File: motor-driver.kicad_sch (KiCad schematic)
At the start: 22 parts, among them J2 SIGNAL, J3 PWR, J4 RTMI, Q5 BSS138

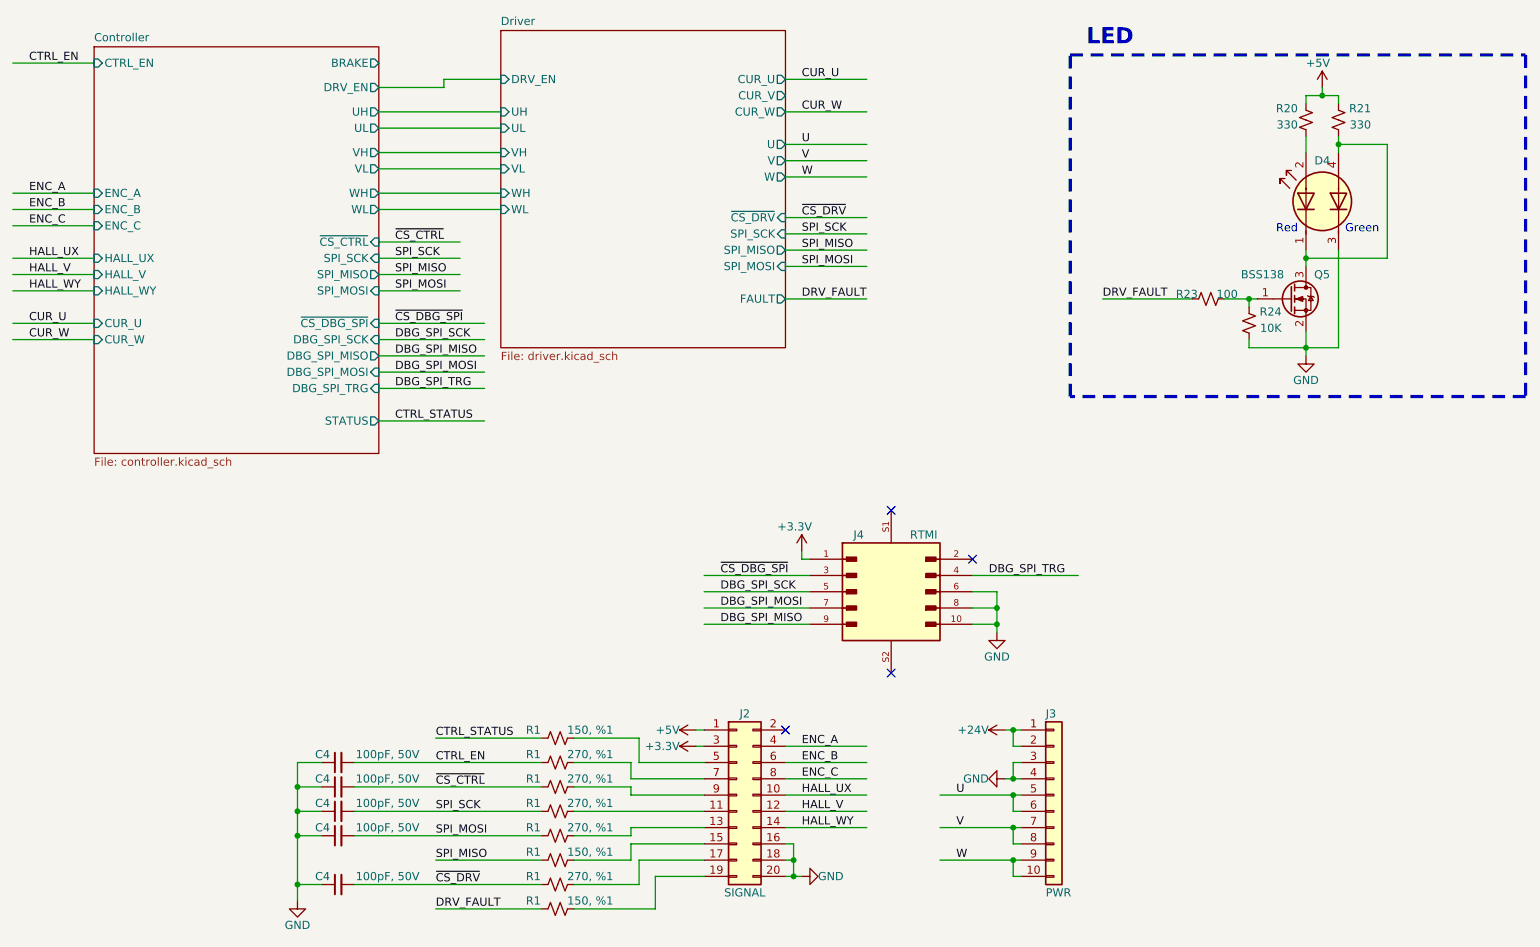
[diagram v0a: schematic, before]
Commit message: Applied the fixes to the pcb.
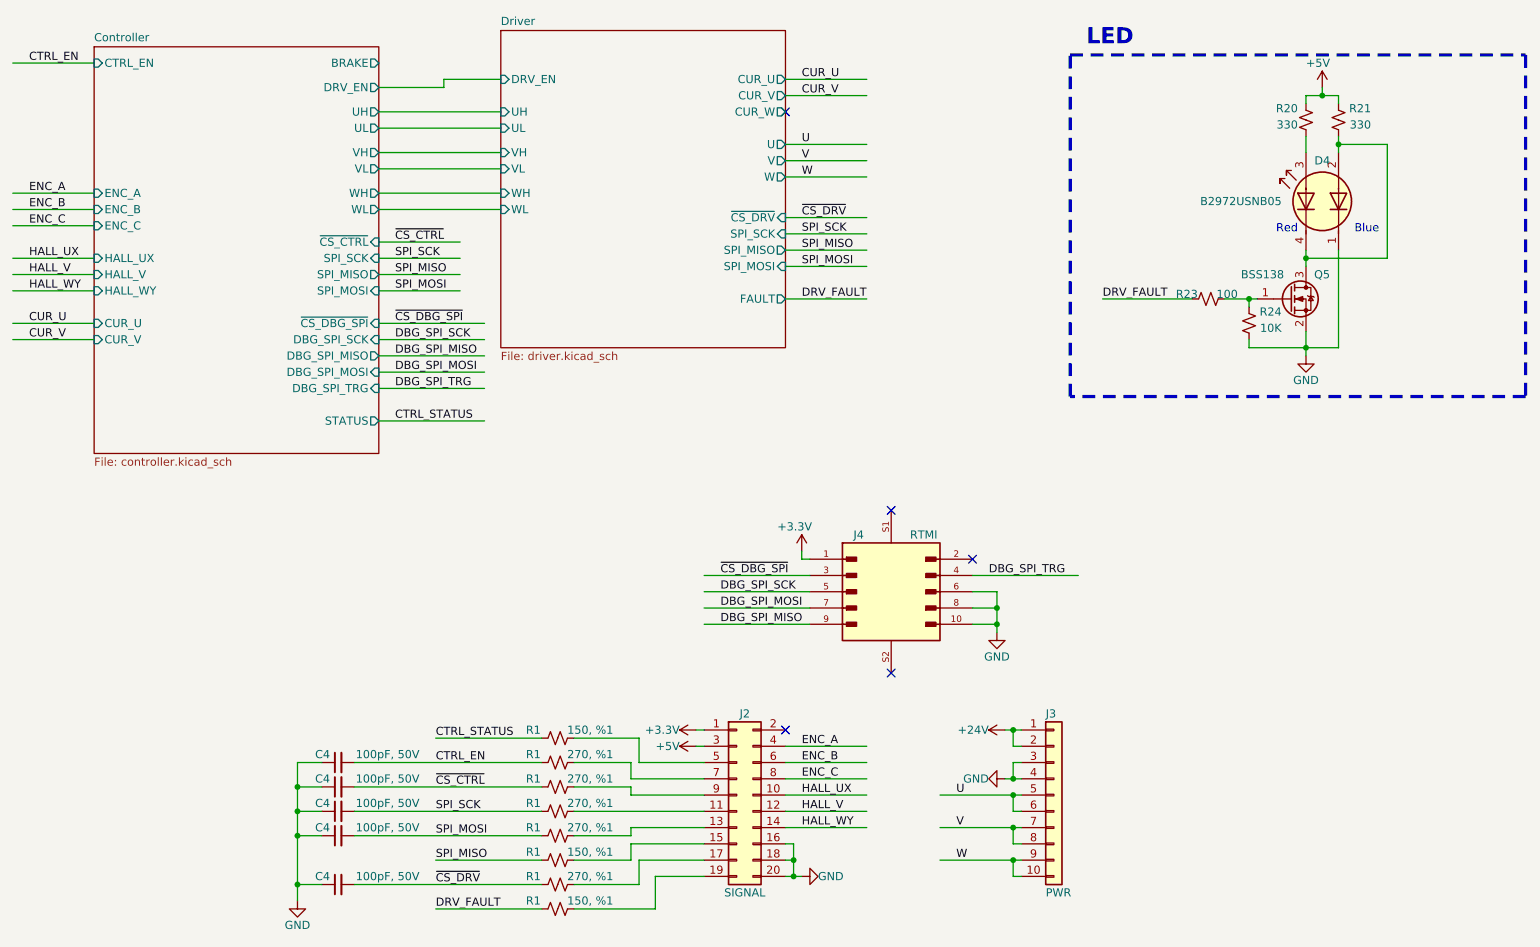
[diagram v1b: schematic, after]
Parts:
- D4: value LED Dual -> B2972USNB05; footprint LED_SMD:LED_Avago_PLCC4_3.2x2.8mm_CW -> B2972USNB05:B2972USNB05; symbol Device:LED_Dual_KAKA -> B2972USNB05:B2972USNB05; MPN LTST-E682KRKGWT -> B2972USNB05D000514U1930
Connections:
- net +3.3V: now also J2.1 (Pin_1); no longer J2.3 (Pin_3)
- net +5V: now also J2.3 (Pin_3); no longer J2.1 (Pin_1)
- net GND: now also D4.1 (K1); no longer D4.3 (A2)
- net at D4.4 (K2), Q5.3 (D), R21.1: now also D4.2 (A1); no longer D4.1 (A1)
- net at R20.1: now also D4.3 (A2); no longer D4.2 (K1)
- no-connect marks 4 -> 5
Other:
- sheet Controller ports: added CUR_V; removed CUR_W
- note added: "Blue"
- note removed: "Green"
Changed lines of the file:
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@@
   (junction (at 224.79 27.94) (diameter 0) (color 0 0 0 0)
   )
+  (no_connect (at 140.97 30.48))
   (no_connect (at 157.48 92.71))
   (no_connect (at 140.97 127))
@@
     (stroke (width 0) (type default))
   )
-  (wire (pts (xy 140.97 30.48) (xy 153.67 30.48))
+  (wire (pts (xy 140.97 27.94) (xy 153.67 27.94))
     (stroke (width 0) (type default))
   )
@@
     (fill (type none))
   )
-  (text "Green" (at 233.68 49.53 0)
+  (text "Blue" (at 233.68 49.53 0)
     (effects (font (size 1.27 1.27)) (justify right bottom))
   )
@@
     (effects (font (size 1.27 1.27)) (justify left bottom))
   )
-  (label "CUR_W" (at 22.86 66.04 0) (fields_autoplaced)
+  (label "CUR_V" (at 22.86 66.04 0) (fields_autoplaced)
     (effects (font (size 1.27 1.27)) (justify left bottom))
   )
@@
     (effects (font (size 1.27 1.27)) (justify left bottom))
   )
-  (label "CUR_W" (at 143.51 30.48 0) (fields_autoplaced)
+  (label "CUR_V" (at 143.51 27.94 0) (fields_autoplaced)
     (effects (font (size 1.27 1.27)) (justify left bottom))
   )
@@
     )
   )
-  (symbol (lib_id "power:+5V") (at 127 127 90) (unit 1)
-    (in_bom yes) (on_board yes) (dnp no)
-    (property "Reference" "#PWR04" (at 130.81 127 0)
-      (effects (font (size 1.27 1.27)) hide)
-    )
-    (property "Value" "+5V" (at 124.46 127 90)
-      (effects (font (size 1.27 1.27)) (justify left))
-    )
-    (property "Footprint" "" (at 127 127 0)
-      (effects (font (size 1.27 1.27)) hide)
-    )
-    (property "Datasheet" "" (at 127 127 0)
+  (symbol (lib_id "power:+5V") (at 127 129.54 90) (unit 1)
+    (in_bom yes) (on_board yes) (dnp no)
+    (property "Reference" "#PWR04" (at 130.81 129.54 0)
+      (effects (font (size 1.27 1.27)) hide)
+    )
+    (property "Value" "+5V" (at 124.46 129.54 90)
+      (effects (font (size 1.27 1.27)) (justify left))
+    )
+    (property "Footprint" "" (at 127 129.54 0)
+      (effects (font (size 1.27 1.27)) hide)
+    )
+    (property "Datasheet" "" (at 127 129.54 0)
       (effects (font (size 1.27 1.27)) hide)
     )
@@
     )
   )
-  (symbol (lib_id "Device:LED_Dual_KAKA") (at 224.79 44.45 90) (unit 1)
+  (symbol (lib_id "B2972USNB05:B2972USNB05") (at 224.79 44.45 90) (unit 1)
     (in_bom yes) (on_board yes) (dnp no)
     (property "Reference" "D4" (at 224.79 38.1 90)
       (effects (font (size 1.27 1.27)))
     )
-    (property "Value" "LED Dual" (at 224.79 50.8 90)
-      (effects (font (size 1.27 1.27)) hide)
-    )
-    (property "Footprint" "LED_SMD:LED_Avago_PLCC4_3.2x2.8mm_CW" (at 224.79 43.688 0)
+    (property "Value" "B2972USNB05" (at 212.09 44.45 90)
+      (effects (font (size 1.27 1.27)))
+    )
+    (property "Footprint" "B2972USNB05:B2972USNB05" (at 224.79 43.688 0)
       (effects (font (size 1.27 1.27)) hide)
     )
@@
       (effects (font (size 1.27 1.27)) hide)
     )
-    (property "MPN" "LTST-E682KRKGWT" (at 224.79 44.45 0)
+    (property "MPN" "B2972USNB05D000514U1930" (at 224.79 44.45 0)
       (effects (font (size 1.27 1.27)) hide)
     )
@@
     )
   )
-  (symbol (lib_id "power:+3.3V") (at 127 129.54 90) (unit 1)
-    (in_bom yes) (on_board yes) (dnp no)
-    (property "Reference" "#PWR054" (at 130.81 129.54 0)
-      (effects (font (size 1.27 1.27)) hide)
-    )
-    (property "Value" "+3.3V" (at 124.46 129.54 90)
-      (effects (font (size 1.27 1.27)) (justify left))
-    )
-    (property "Footprint" "" (at 127 129.54 0)
-      (effects (font (size 1.27 1.27)) hide)
-    )
-    (property "Datasheet" "" (at 127 129.54 0)
+  (symbol (lib_id "power:+3.3V") (at 127 127 90) (unit 1)
+    (in_bom yes) (on_board yes) (dnp no)
+    (property "Reference" "#PWR054" (at 130.81 127 0)
+      (effects (font (size 1.27 1.27)) hide)
+    )
+    (property "Value" "+3.3V" (at 124.46 127 90)
+      (effects (font (size 1.27 1.27)) (justify left))
+    )
+    (property "Footprint" "" (at 127 127 0)
+      (effects (font (size 1.27 1.27)) hide)
+    )
+    (property "Datasheet" "" (at 127 127 0)
       (effects (font (size 1.27 1.27)) hide)
     )
@@
       (effects (font (size 1.27 1.27)) (justify right))
     )
-    (pin "CUR_W" input (at 33.02 66.04 180)
-      (effects (font (size 1.27 1.27)) (justify left))
-    )
     (pin "CUR_U" input (at 33.02 63.5 180)
       (effects (font (size 1.27 1.27)) (justify left))
@@
       (effects (font (size 1.27 1.27)) (justify right))
     )
-    (instances
+    (pin "CUR_V" input (at 33.02 66.04 180)
+      (effects (font (size 1.27 1.27)) (justify left))
+    )
+    (instances

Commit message: Small improvements.
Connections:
- net ENC_A: now also J2.2 (Pin_2); no longer J2.4 (Pin_4)
- net ENC_B: now also J2.4 (Pin_4); no longer J2.6 (Pin_6)
- net ENC_C: now also J2.6 (Pin_6); no longer J2.8 (Pin_8)
- net GND: now also J2.14 (Pin_14)
- net HALL_UX: now also J2.8 (Pin_8); no longer J2.10 (Pin_10)
- net HALL_V: now also J2.10 (Pin_10); no longer J2.12 (Pin_12)
- net HALL_WY: now also J2.12 (Pin_12); no longer J2.14 (Pin_14)
- no-connect marks 5 -> 4

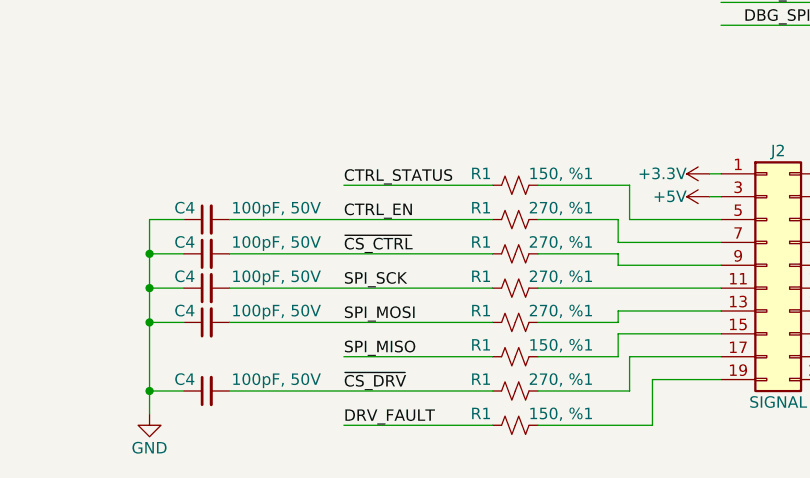
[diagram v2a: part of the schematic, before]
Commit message: Optimize the BOM.
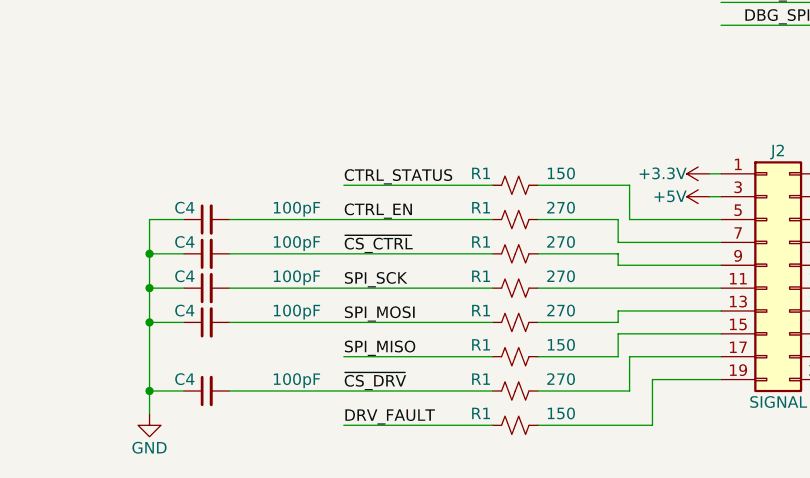
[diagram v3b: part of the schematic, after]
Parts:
- C4: value 100pF, 50V -> 100pF
- R1: value 270, %1 -> 270
- R1: value 150, %1 -> 150
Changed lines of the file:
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@@
       (effects (font (size 1.27 1.27)) (justify left))
     )
-    (property "Value" "100pF, 50V" (at 83.82 149.86 90)
+    (property "Value" "100pF" (at 83.82 149.86 90)
       (effects (font (size 1.27 1.27)) (justify left))
     )
@@
       (effects (font (size 1.27 1.27)) (justify left))
     )
-    (property "Value" "100pF, 50V" (at 83.82 134.62 90)
+    (property "Value" "100pF" (at 83.82 134.62 90)
       (effects (font (size 1.27 1.27)) (justify left))
     )
@@
       (effects (font (size 1.27 1.27)))
     )
-    (property "Value" "270, %1" (at 110.49 138.43 90)
+    (property "Value" "270" (at 110.49 138.43 90)
       (effects (font (size 1.27 1.27)))
     )
@@
       (effects (font (size 1.27 1.27)))
     )
-    (property "Value" "270, %1" (at 110.49 134.62 90)
+    (property "Value" "270" (at 110.49 134.62 90)
       (effects (font (size 1.27 1.27)))
     )
@@
       (effects (font (size 1.27 1.27)))
     )
-    (property "Value" "150, %1" (at 110.49 146.05 90)
+    (property "Value" "150" (at 110.49 146.05 90)
       (effects (font (size 1.27 1.27)))
     )
@@
       (effects (font (size 1.27 1.27)))
     )
-    (property "Value" "270, %1" (at 110.49 142.24 90)
+    (property "Value" "270" (at 110.49 142.24 90)
       (effects (font (size 1.27 1.27)))
     )
@@
       (effects (font (size 1.27 1.27)))
     )
-    (property "Value" "270, %1" (at 110.49 130.81 90)
+    (property "Value" "270" (at 110.49 130.81 90)
       (effects (font (size 1.27 1.27)))
     )
@@
       (effects (font (size 1.27 1.27)))
     )
-    (property "Value" "150, %1" (at 110.49 127 90)
+    (property "Value" "150" (at 110.49 127 90)
       (effects (font (size 1.27 1.27)))
     )
@@
       (effects (font (size 1.27 1.27)) (justify left))
     )
-    (property "Value" "100pF, 50V" (at 83.82 130.81 90)
+    (property "Value" "100pF" (at 83.82 130.81 90)
       (effects (font (size 1.27 1.27)) (justify left))
     )
@@
       (effects (font (size 1.27 1.27)) (justify left))
     )
-    (property "Value" "100pF, 50V" (at 83.82 138.43 90)
+    (property "Value" "100pF" (at 83.82 138.43 90)
       (effects (font (size 1.27 1.27)) (justify left))
     )
@@
       (effects (font (size 1.27 1.27)) (justify left))
     )
-    (property "Value" "100pF, 50V" (at 83.82 142.24 90)
+    (property "Value" "100pF" (at 83.82 142.24 90)
       (effects (font (size 1.27 1.27)) (justify left))
     )
@@
       (effects (font (size 1.27 1.27)))
     )
-    (property "Value" "270, %1" (at 110.49 149.86 90)
+    (property "Value" "270" (at 110.49 149.86 90)
       (effects (font (size 1.27 1.27)))
     )
@@
       (effects (font (size 1.27 1.27)))
     )
-    (property "Value" "150, %1" (at 110.49 153.67 90)
-      (effects (font (size 1.27 1.27)))
-    )
+    (property "Value" "150" (at 110.49 153.67 90)
+      (effects (font (size 1.27 1.27)))
+    )
